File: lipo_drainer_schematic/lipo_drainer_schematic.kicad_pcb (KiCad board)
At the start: 2 copper layers, 59 parts, among them J1 BATT, J2 FAN, J3 Vcal, J4 128x64_OLED, J5 Gcal, J6 Ical, J7 Heatsink Temp (for MCP7901), Q1 MMBT3904, Q10 G700P06T, Q11 G700P06T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

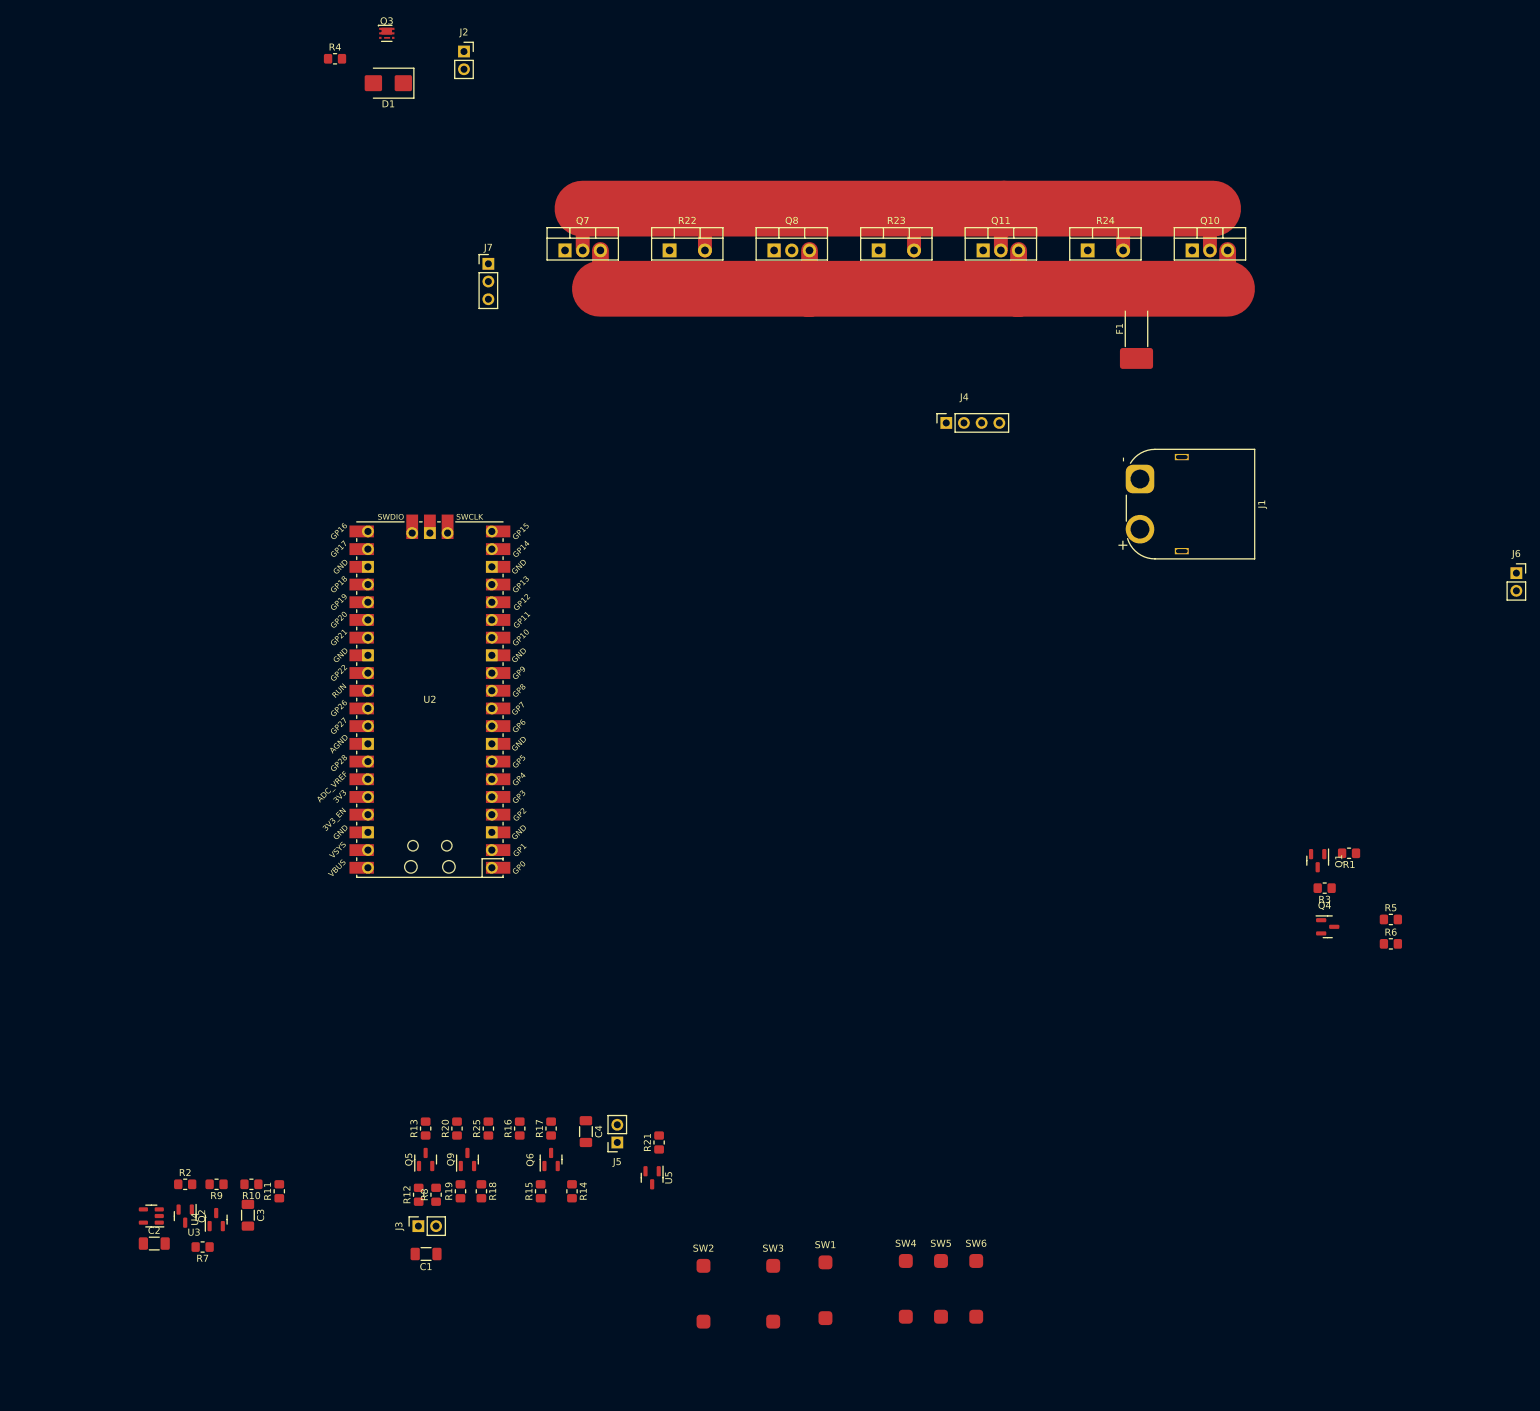
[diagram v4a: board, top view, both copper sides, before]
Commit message: Starting to group PCB layout into logical sections.
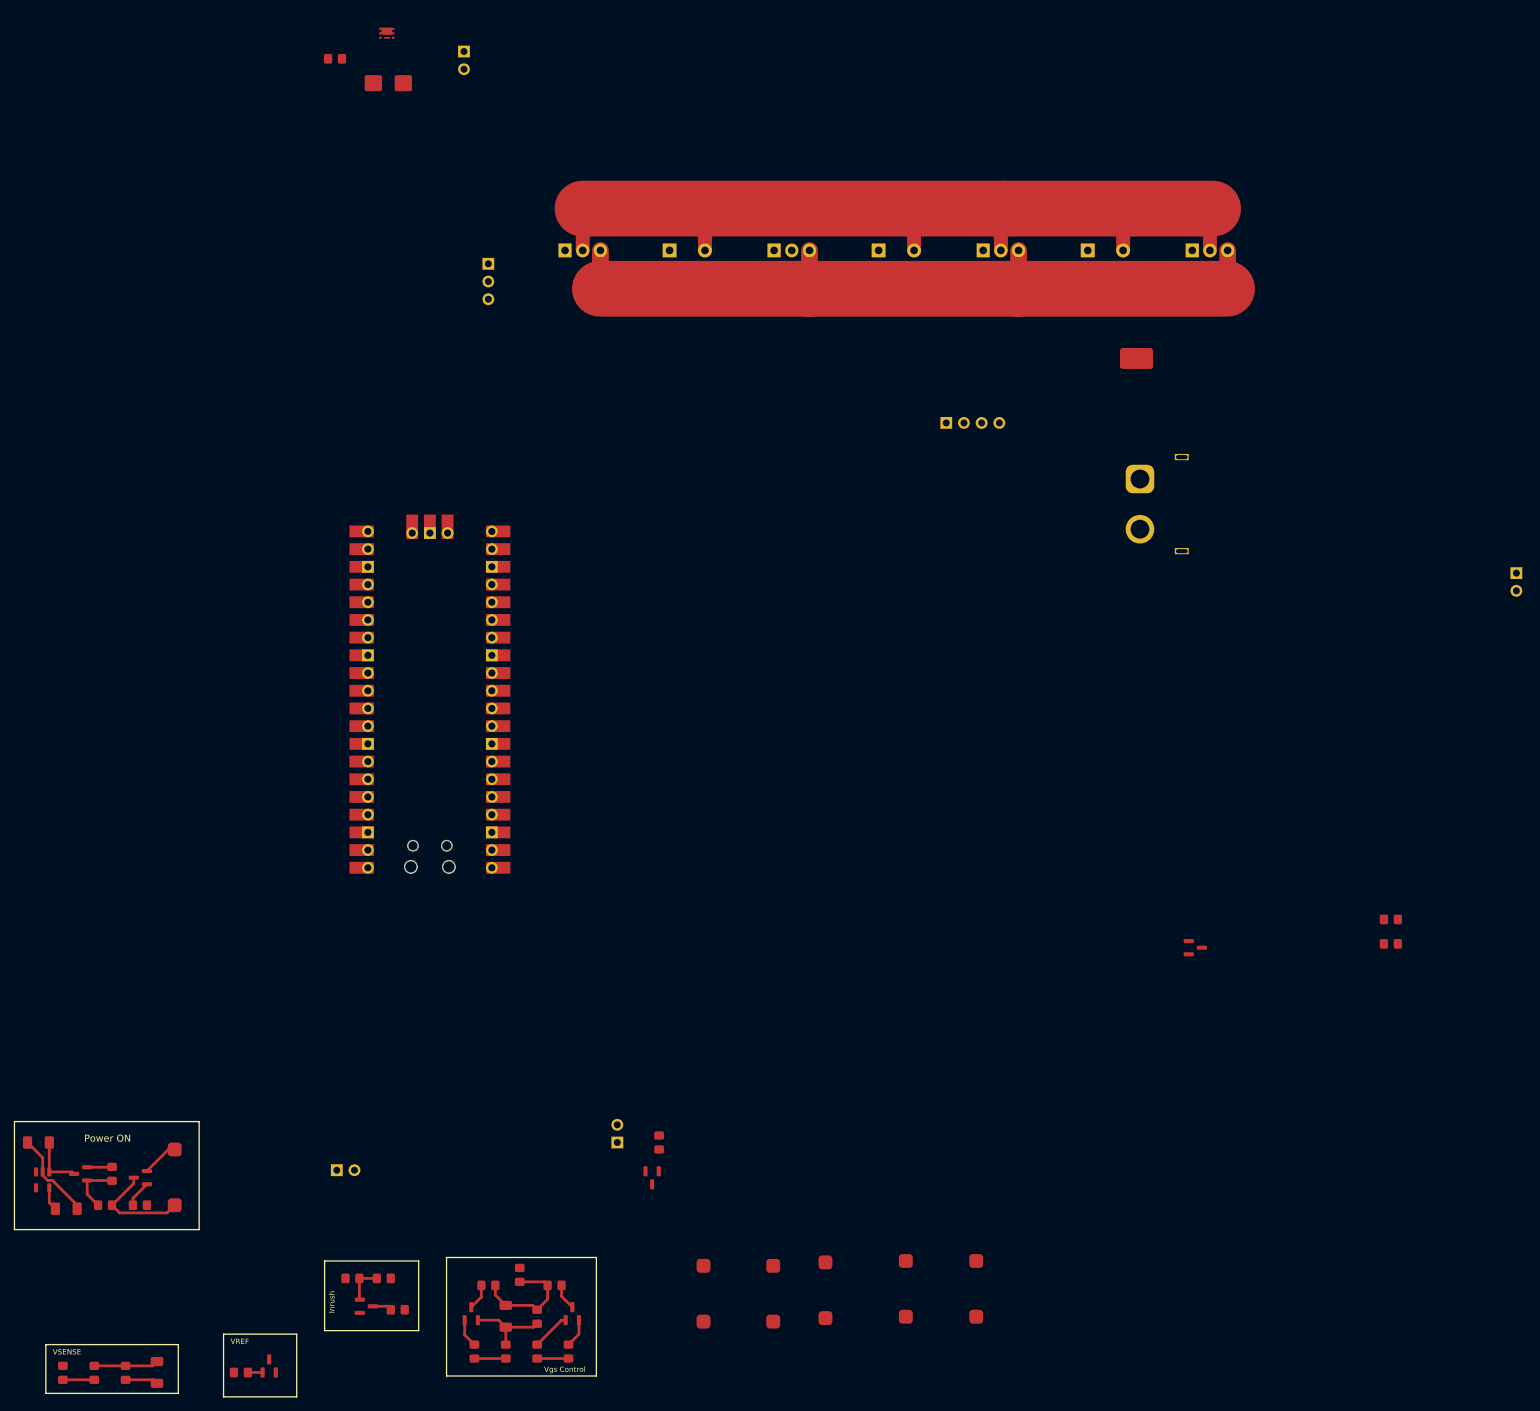
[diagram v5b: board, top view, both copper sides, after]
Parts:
- moved R3 180.8 mm to (-15.0, 229.0), turned to 0 degrees
- moved R1 180.7 mm to (-10.0, 229.0)
- moved Q1 175.0 mm to (-9.94, 225.1), turned to 180 degrees
- moved SW5 111.1 mm to (-5.00, 229.0)
- moved C1 57.9 mm to (-24.6, 220.0)
- moved R10 35.2 mm to (-16.6, 253.1), turned to -90 degrees
- moved R9 34.9 mm to (-21.1, 253.1), turned to 90 degrees
- moved R11 34.1 mm to (-12.1, 253.1)
- moved C4 28.9 mm to (42.5, 244.9)
- moved R25 27.9 mm to (47.0, 245.0)
- moved Q9 26.8 mm to (52.0, 244.6)
- moved R20 26.5 mm to (49.5, 240.5), turned to 180 degrees
- moved R13 26.3 mm to (27.0, 244.0), turned to 0 degrees
- moved R18 26.2 mm to (51.5, 250.0)
- moved C3 26.1 mm to (-7.55, 253.0)
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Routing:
- net GND: track 0.00 -> 38.6 mm
- net /FET-G: track 0.00 -> 16.6 mm
- net /ON: track 0.00 -> 15.2 mm
- net /VOLT: track 0.00 -> 9.26 mm
- net /VHIGH: track 0.00 -> 7.90 mm
- net Net-(Q2-G): track 0.00 -> 7.78 mm
- net Net-(Q5-G): track 0.00 -> 5.58 mm
- net Net-(Q9-B): track 0.00 -> 5.55 mm
- net Net-(R10-Pad2): track 0.00 -> 4.50 mm
- net /SLOW: track 0.00 -> 4.50 mm
- net /FAST: track 0.00 -> 4.50 mm
- net Net-(Q6-B): track 0.00 -> 4.08 mm
- net Net-(Q1-B): track 0.00 -> 3.83 mm
- net Net-(Q9-C): track 0.00 -> 3.77 mm
- net Net-(Q6-C): track 0.00 -> 3.73 mm
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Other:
- board text added: "Inrush"
- board text added: "Power ON"
- board text added: "VREF"
- board text added: "VSENSE"
- board text added: "Vgs Control"

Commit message: Changed button definitions.
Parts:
- removed SW6: RUN, Matt:SMD_Button_6mm_3_5mm
- SW1: value BT1 -> OFF
- SW2: value BT2 -> NEXT
- SW3: value BT3 -> OK
- SW4: value BT4 -> RUN
- moved R4 216.2 mm to (132.0, 248.2)
- moved Q3 210.2 mm to (122.5, 247.3), turned to 90 degrees
- moved D1 199.8 mm to (117.5, 245.4), turned to 90 degrees
- moved J2 196.1 mm to (112.5, 244.3)
- moved R5 73.8 mm to (127.0, 248.3), turned to 180 degrees
- moved SW5 69.6 mm to (64.0, 238.0), turned to 180 degrees
- moved R6 67.4 mm to (127.0, 243.8)
- moved SW4 61.0 mm to (50.0, 210.0)
- moved J1 57.4 mm to (188.0, 106.7)
- moved Q4 53.5 mm to (131.9, 244.8), turned to -90 degrees
- moved J4 51.4 mm to (153.4, 136.0)
- moved SW1 16.1 mm to (74.0, 238.0), turned to 180 degrees
- moved SW2 15.2 mm to (84.0, 238.0), turned to 180 degrees
- moved SW3 15.2 mm to (94.0, 238.0), turned to 180 degrees
- moved J7 2.16 mm to (39.0, 92.0), turned to 90 degrees
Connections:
- net /B1 renamed /OFF
- net /B2 renamed /NEXT
- net /B3 renamed /OK
- SW4 pad 1: /B4 -> Net-(U2-RUN)
- U2 pad 12: /B4 -> unconnected-(U2-GPIO9-Pad12)
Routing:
- net GND: track 38.6 -> 83.0 mm
- net /FAN+: track 0.00 -> 10.1 mm
- net /ON: track 15.2 -> 6.80 mm
- net Net-(Q3-G): track 0.00 -> 8.21 mm
- net Net-(Q4-C): track 0.00 -> 5.08 mm
- net /BAT+: track 3.58 -> 8.27 mm
- net Net-(Q4-B): track 0.00 -> 4.48 mm
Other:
- board text added: "Controls"
- board text added: "Fan Control"

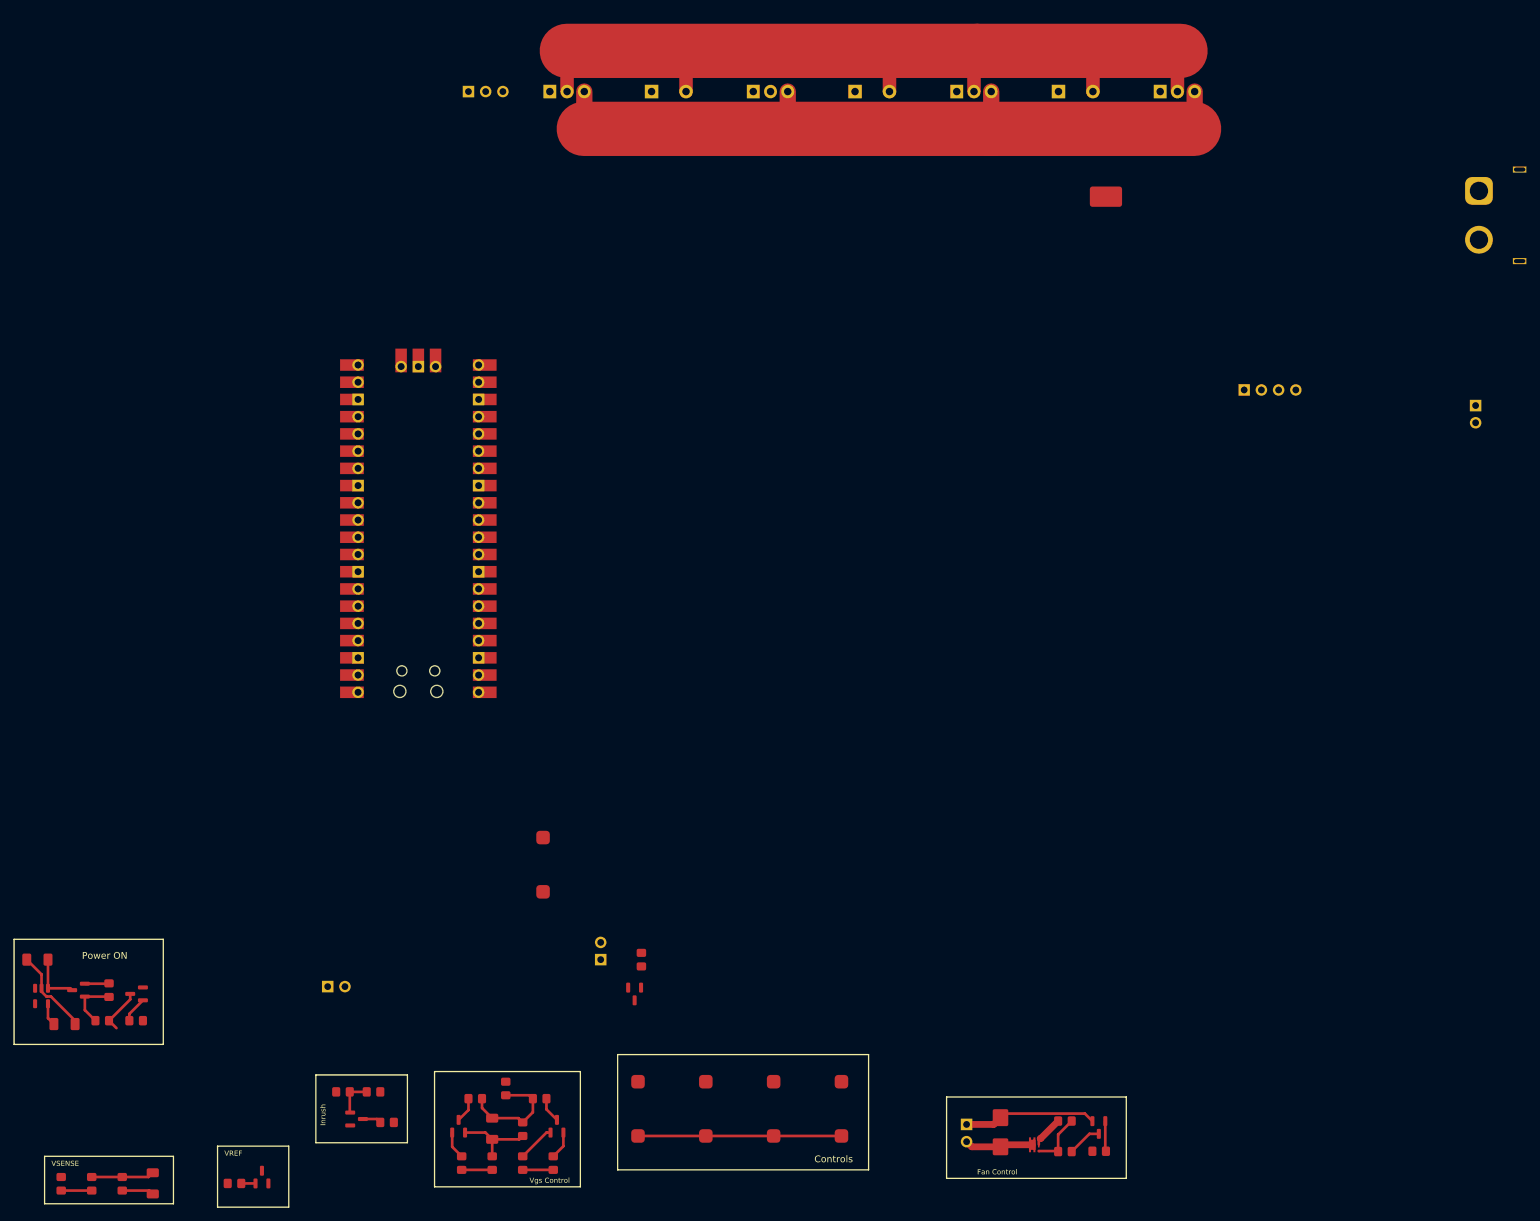
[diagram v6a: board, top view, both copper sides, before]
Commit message: Placed subblocks in PCB
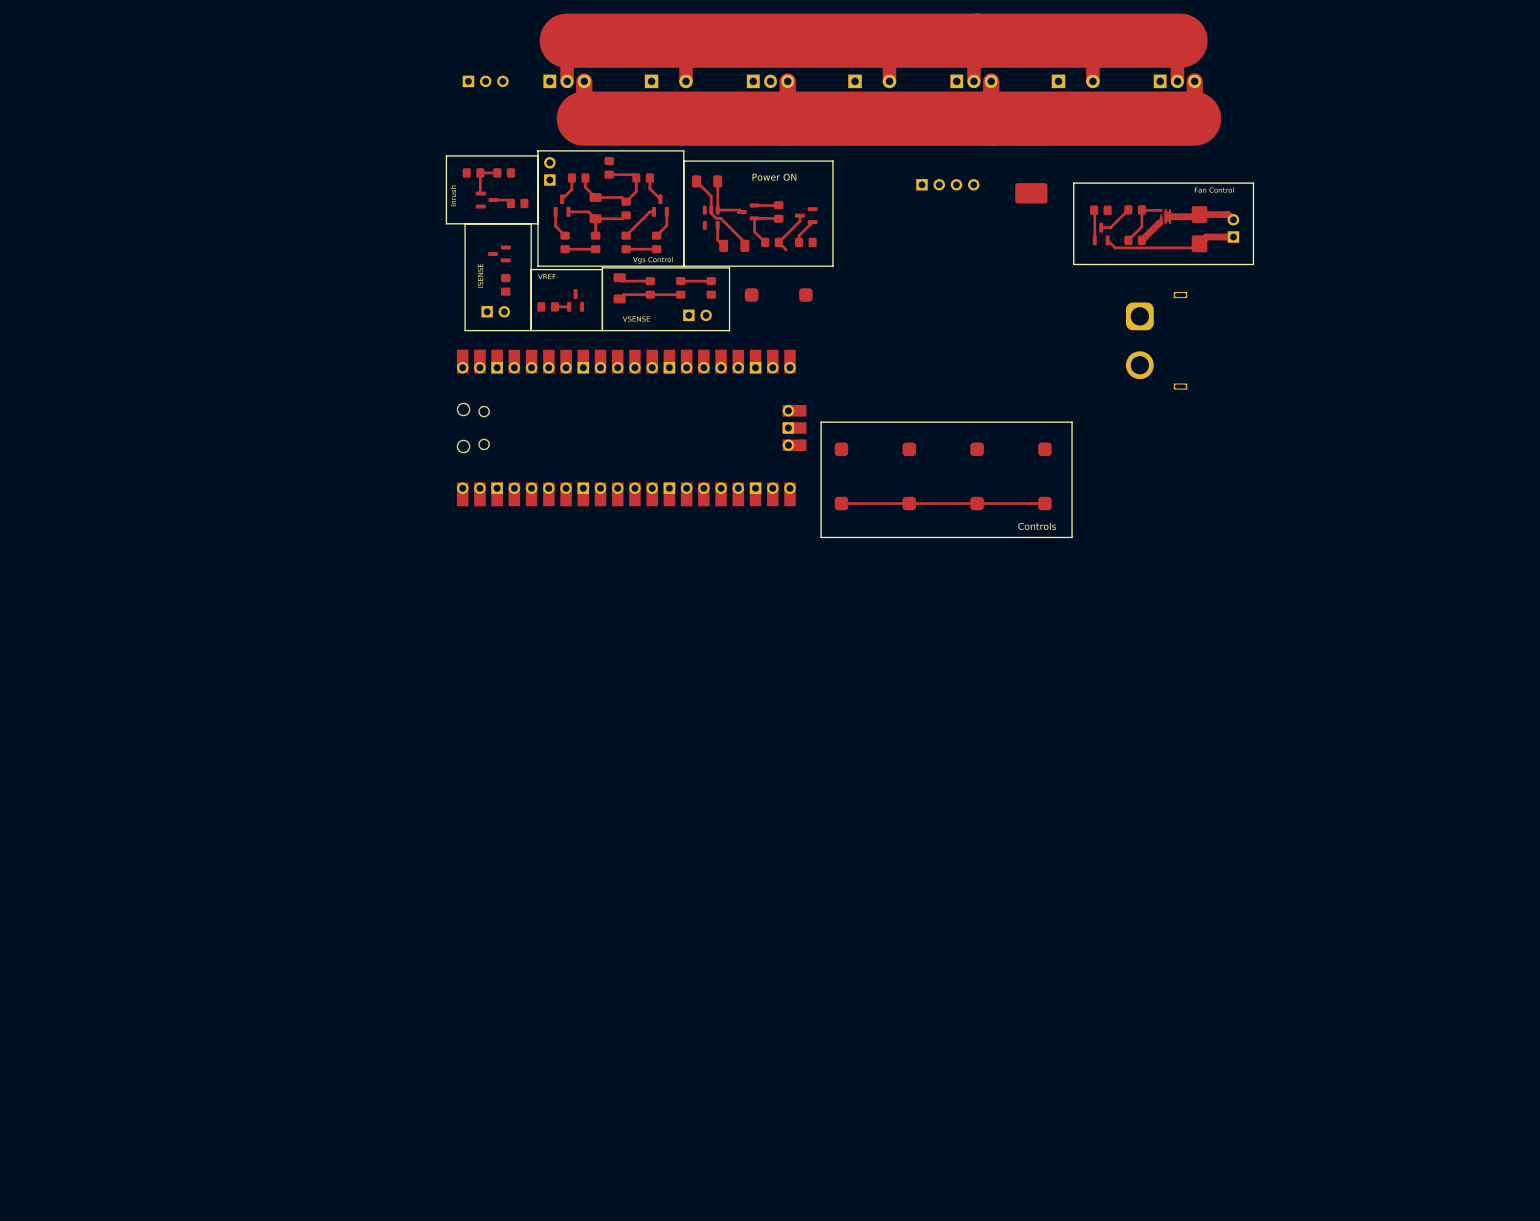
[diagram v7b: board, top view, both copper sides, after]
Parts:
- moved R9 163.2 mm to (74.8, 121.0), turned to -90 degrees
- moved R10 158.1 mm to (70.3, 121.0), turned to 90 degrees
- moved R11 153.3 mm to (65.8, 121.0), turned to -90 degrees
- moved C1 151.4 mm to (74.2, 105.2)
- moved C2 151.4 mm to (78.2, 114.8)
- moved Q1 151.4 mm to (88.8, 110.3)
- moved Q2 151.4 mm to (80.2, 109.8)
- moved R1 151.4 mm to (88.8, 114.2)
- moved R2 151.4 mm to (84.8, 109.8)
- moved R3 151.4 mm to (83.8, 114.2)
- moved U3 151.4 mm to (74.8, 110.6)
- moved C3 148.9 mm to (61.3, 121.0), turned to 90 degrees
- moved J6 146.4 mm to (41.8, 124.5), turned to 90 degrees
- moved R5 139.2 mm to (137.3, 109.5), turned to 0 degrees
- moved R4 138.8 mm to (132.2, 109.5), turned to 180 degrees
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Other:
- board text added: "ISENSE"
